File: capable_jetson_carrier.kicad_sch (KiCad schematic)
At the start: 3 parts

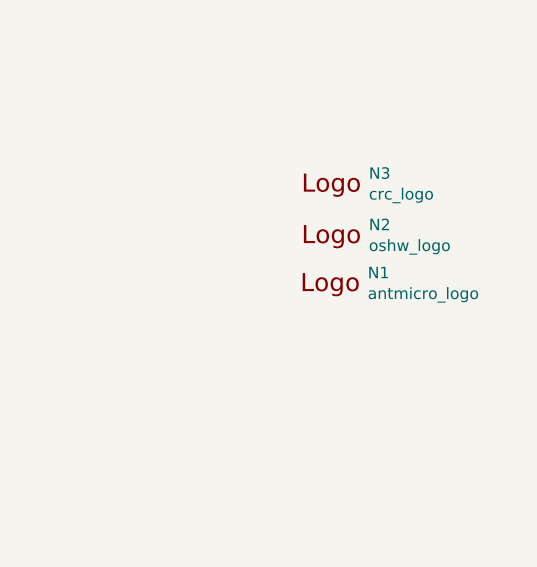
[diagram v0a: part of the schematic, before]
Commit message: Checkpoint.  New camera connectors.  Change to 2242 NVMe drive (not routed yet).
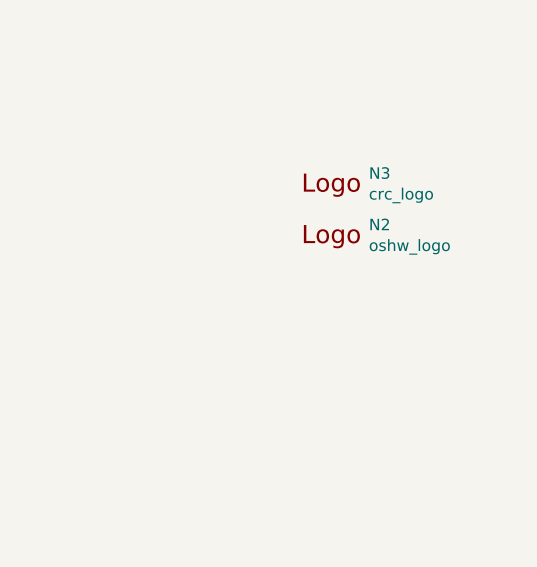
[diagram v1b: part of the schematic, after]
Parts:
- removed N1: antmicro_logo, jetson-nano-baseboard-footprints:antmicro-logo, symbol jetson-nano-baseboard:antmicro_logo
- N2, N3: now left out of the parts list

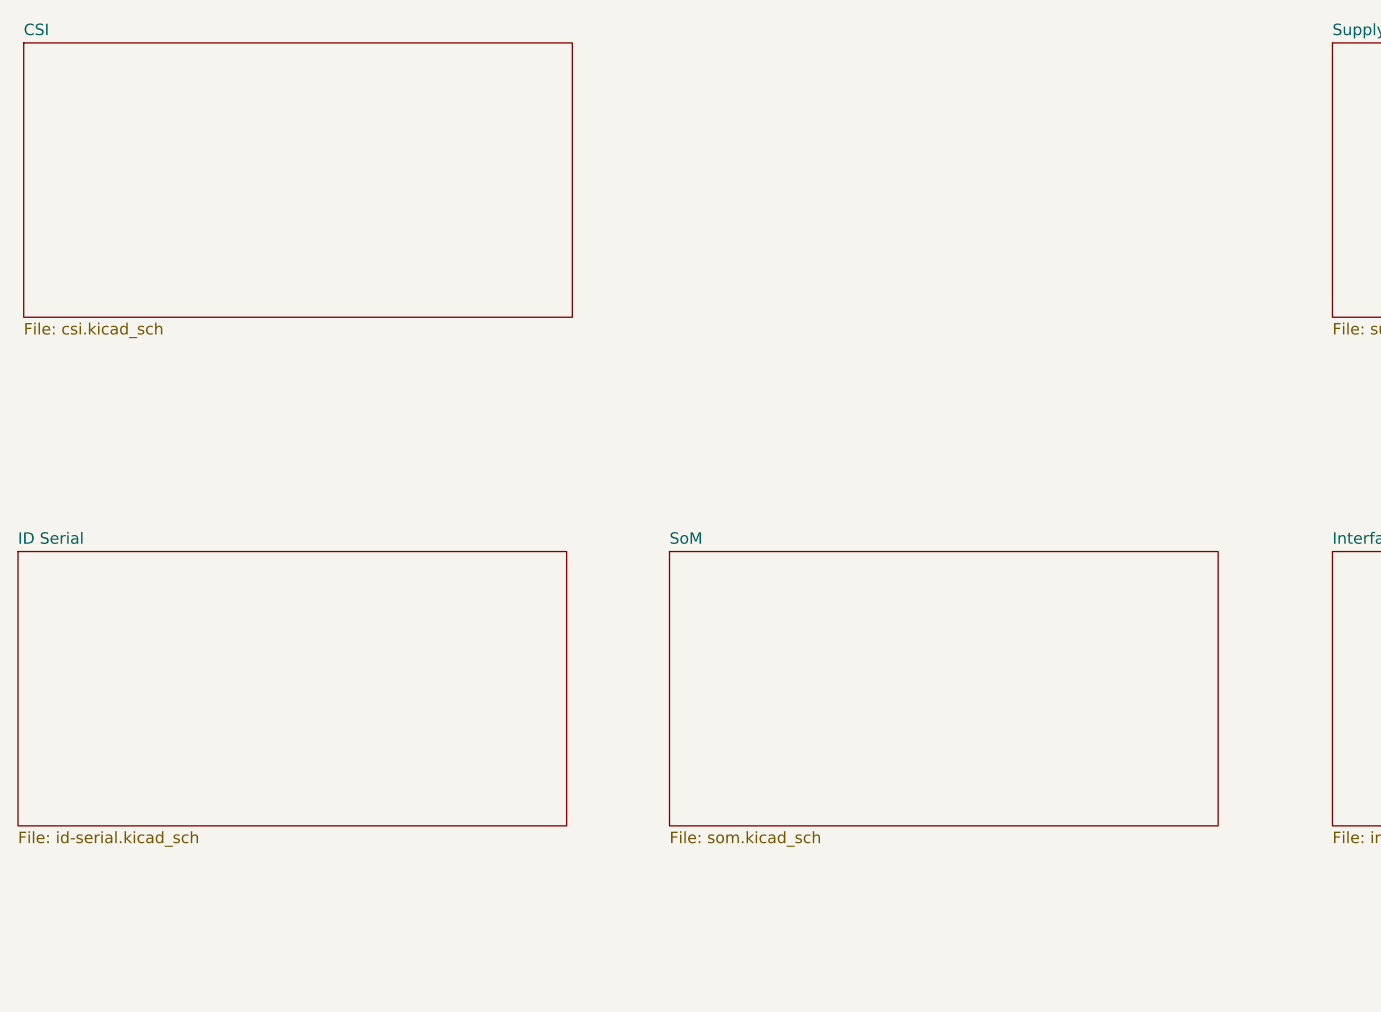
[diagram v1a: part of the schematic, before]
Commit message: Start of trigger FPGA.  Better layout
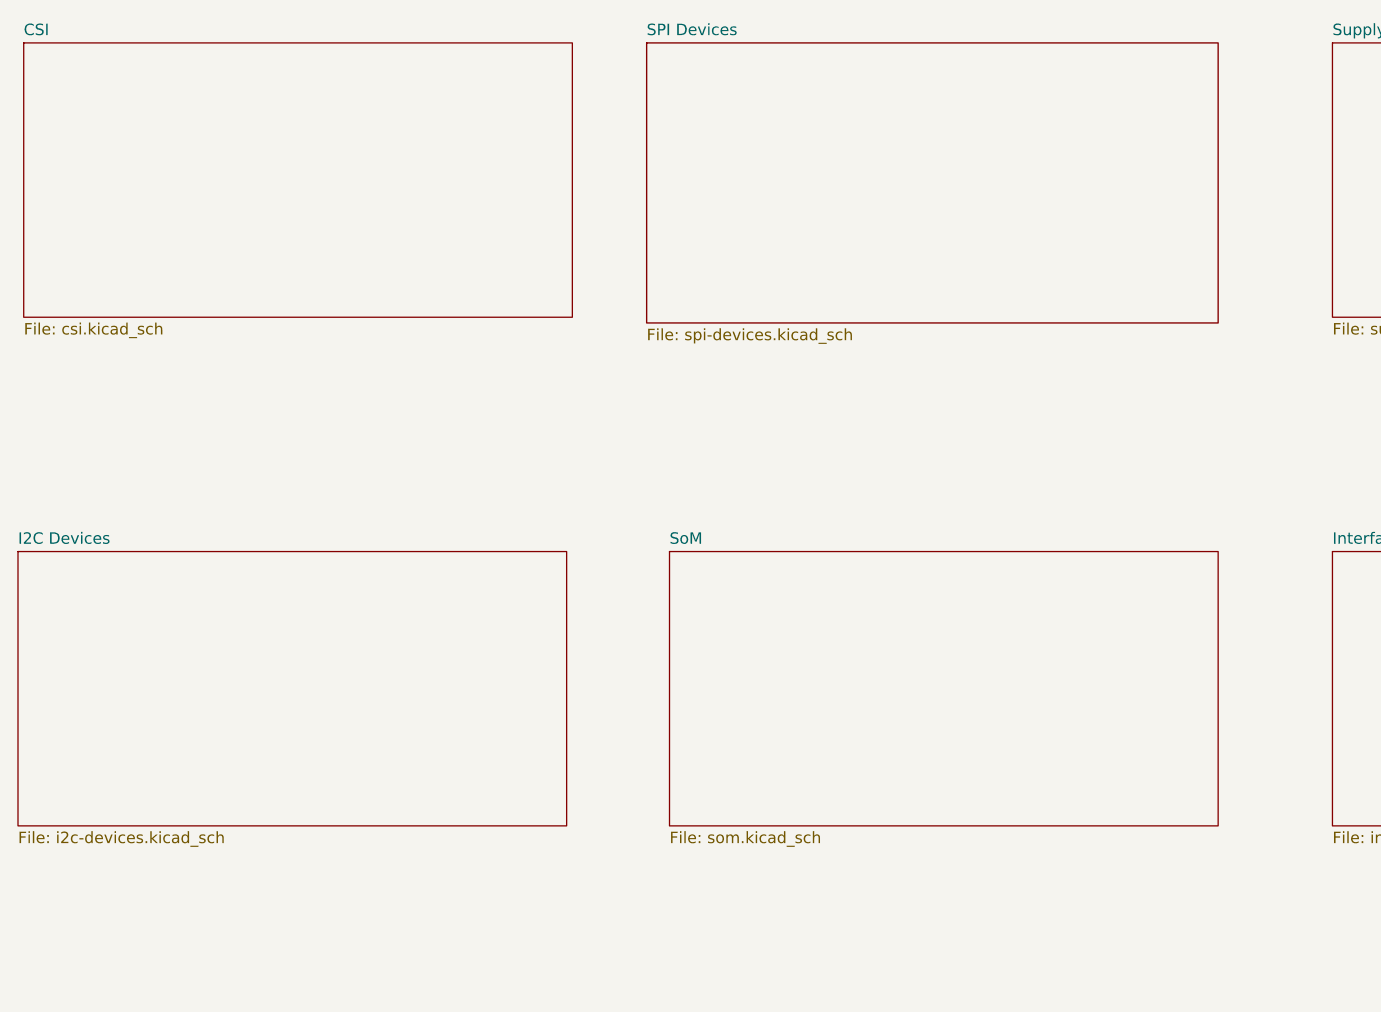
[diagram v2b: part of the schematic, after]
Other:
- sheet ID Serial renamed I2C Devices
- added sheet SPI Devices (spi-devices.kicad_sch)
- sheet I2C Devices: file id-serial.kicad_sch -> i2c-devices.kicad_sch
